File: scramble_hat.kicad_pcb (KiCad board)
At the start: 4 copper layers, 51.4 x 21.1 mm, 75 parts, among them J1 NCJ6FA-H, J2 TRRS PJ-3X4S (CTIA, bottom-si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, J3 Carrier LEFT 1-7, J4 Carrier RIGHT 1-7, J5 VDD_PoE / PGND, J6 I2C 3V3/AGND/SDA/SCL, K1 KAQY214S, K2 KAQY214S, Q1 DMP3098 (P-FET 60V), SW1 SS-12D00-G3, U1 ES8389, U2 TPS7A2033, U3 TLV9061, U4 74HC4053

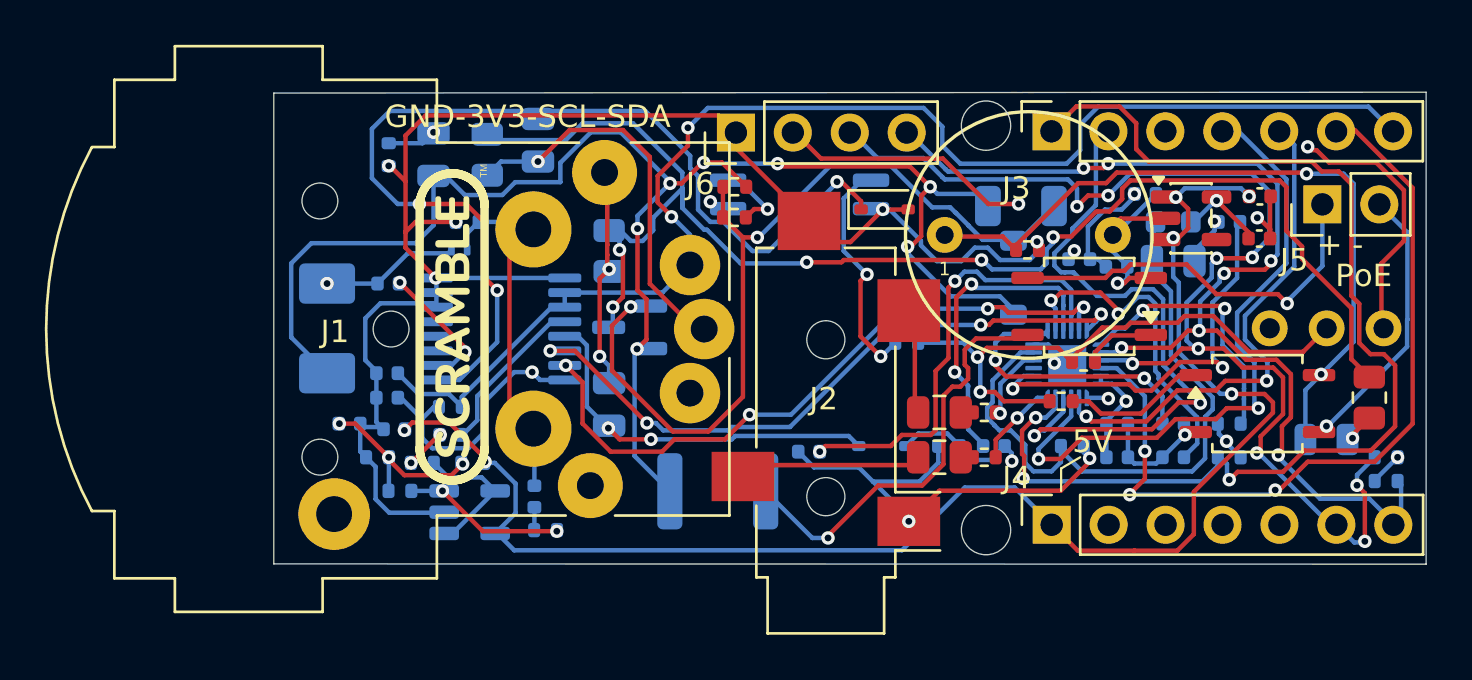
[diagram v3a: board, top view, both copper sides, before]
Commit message: sw1 optional: DNP by default (phantom-less builds); J7/R27 placed+routed; restore pos-file exclusions; regen fab + docs
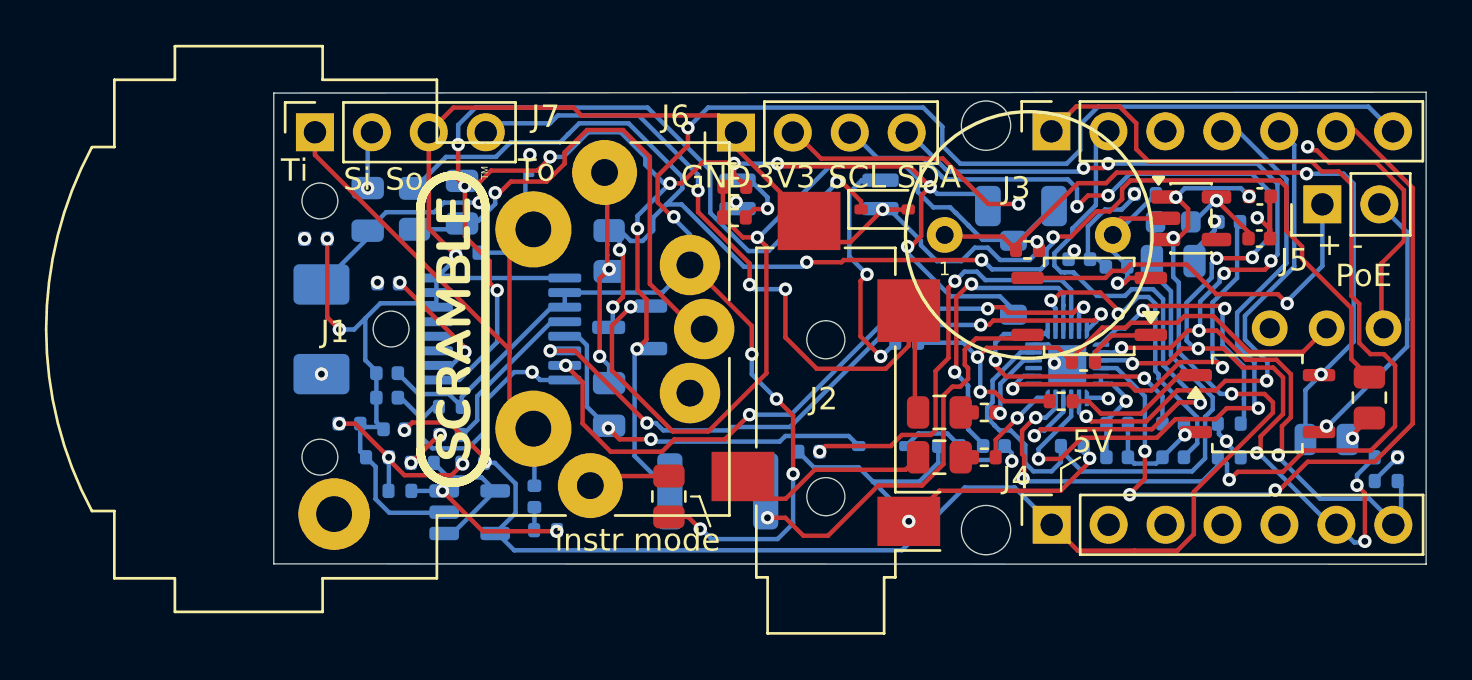
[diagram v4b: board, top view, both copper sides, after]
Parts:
- added J7: TO EURORACK MODULE (alt. to J1), Connector_PinSocket_2.54mm:PinSocket_1x04_P2.54mm_Vertical, F.Cu at (82.7, 82.0)
- added R27: R0 (force instrument mode), Resistor_SMD:R_0805_2012Metric, F.Cu at (98.5, 98.2)
- moved R25 4.96 mm to (82.8, 86.8), turned to 0 degrees
- moved D9 4.87 mm to (92.2, 83.5), turned to 90 degrees
- moved C11 4.37 mm to (89.3, 85.1)
- moved R6 4.04 mm to (87.2, 85.4)
- moved C17 3.82 mm to (85.1, 85.4)
- moved R26 1.37 mm to (89.5, 87.4)
- moved OK1 0.42 mm to (104.8, 84.8)
- moved D6 0.25 mm to (83.0, 90.8), turned to 90 degrees
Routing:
- net HP_L_OUT: track 3.20 -> 31.8 mm, vias 0 -> 3
- net DET: track 59.7 -> 79.4 mm, vias 2 -> 6
- net GTIP: track 15.5 -> 28.3 mm
- net V_FILT: track 70.9 -> 61.5 mm, vias 7 -> 9
- net MIC1N_XLR: track 45.3 -> 37.9 mm, vias 3 -> 4
- net XLR3_COLD: track 17.5 -> 22.3 mm
- net V_PHANTOM: track 62.9 -> 66.0 mm
- net PGND: track 42.2 -> 39.9 mm, vias 5 -> 8
- net AGND: track 113.9 -> 115.8 mm
- net HP_R_OUT: track 7.69 -> 8.99 mm
- net Q1_GATE: track 37.9 -> 38.8 mm
- net V_PoE: track 19.1 -> 18.4 mm
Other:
- board text added: "3V3"
- board text added: "GND"
- board text added: "Hat-trik v4"
- board text added: "SCL"
- board text added: "SDA"
- board text added: "Si"
- board text added: "So"
- board text added: "Ti"
- board text added: "To"
- board text removed: "GND-3V3-SCL-SDA"
- board text removed: "Hat-trik v3"

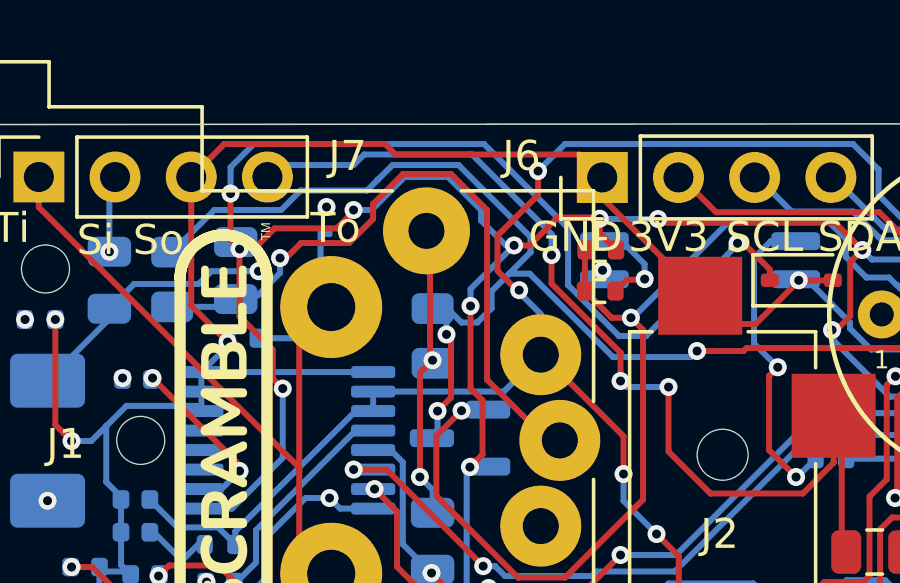
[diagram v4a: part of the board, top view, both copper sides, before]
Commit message: pcb: widen HP_L_OUT to MIC1N_XLR spacing on B.Cu; regen fab
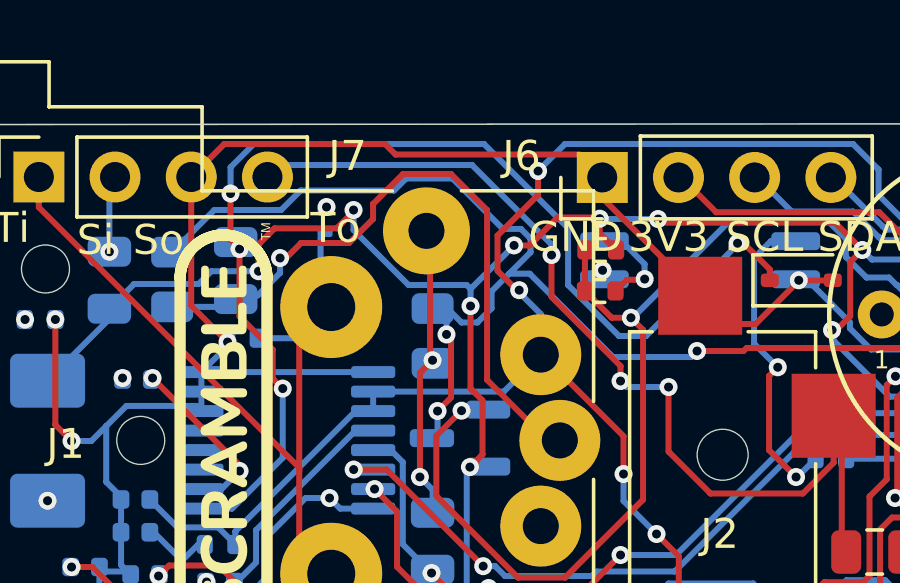
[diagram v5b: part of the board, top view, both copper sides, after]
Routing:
- net V_FILT: track 61.5 -> 60.0 mm
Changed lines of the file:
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@@
 	)
 	(segment
-		(start 102.1 87.855883)
-		(end 99.8 85.555883)
+		(start 109.474 91.3638)
+		(end 109.474 94.3532)
 		(width 0.2)
 		(layer "F.Cu")
@@
 	)
 	(segment
-		(start 109.474 91.3638)
-		(end 109.474 94.3532)
+		(start 109.2032 89.9582)
+		(end 109.2032 91.524618)
 		(width 0.2)
 		(layer "F.Cu")
@@
 	)
 	(segment
-		(start 109.2032 89.9582)
-		(end 109.2032 91.524618)
+		(start 102.1 88.8)
+		(end 102.1 88.3)
 		(width 0.2)
 		(layer "F.Cu")
@@
 	)
 	(segment
-		(start 99.8 85.555883)
+		(start 99.8 86)
 		(end 99.8 84.6)
 		(width 0.2)
@@
 	)
 	(segment
-		(start 102.1 88.8)
-		(end 102.1 87.855883)
+		(start 102.1 88.3)
+		(end 99.8 86)
 		(width 0.2)
 		(layer "F.Cu")
@@
 	)
 	(segment
-		(start 90.73 81.6)
-		(end 90.33 82)
-		(width 0.2)
-		(layer "B.Cu")
-		(net "HP_L_OUT")
-	)
-	(segment
-		(start 93.2 81.6)
-		(end 90.73 81.6)
-		(width 0.2)
-		(layer "B.Cu")
-		(net "HP_L_OUT")
-	)
-	(segment
 		(start 99.8 84.6)
-		(end 99.8 83.9)
+		(end 99.8 84.25)
 		(width 0.2)
 		(layer "B.Cu")
@@
 	)
 	(segment
-		(start 97.15 81.25)
-		(end 93.55 81.25)
+		(start 90.73 81.6)
+		(end 90.33 82)
 		(width 0.2)
 		(layer "B.Cu")
@@
 	)
 	(segment
-		(start 93.55 81.25)
-		(end 93.2 81.6)
+		(start 103.7 89)
+		(end 102.3 89)
 		(width 0.2)
 		(layer "B.Cu")
@@
 	)
 	(segment
-		(start 103.7 89)
-		(end 102.3 89)
+		(start 97.15 81.6)
+		(end 90.73 81.6)
 		(width 0.2)
 		(layer "B.Cu")
@@
 	)
 	(segment
-		(start 99.8 83.9)
-		(end 97.15 81.25)
+		(start 102.3 89)
+		(end 102.1 88.8)
 		(width 0.2)
 		(layer "B.Cu")
@@
 	)
 	(segment
-		(start 102.3 89)
-		(end 102.1 88.8)
+		(start 99.8 84.25)
+		(end 97.15 81.6)
 		(width 0.2)
 		(layer "B.Cu")
@@
 	)
 	(segment
+		(start 98.18 83.73)
+		(end 96.5 82.05)
+		(width 0.2)
+		(layer "B.Cu")
+		(net "V_PHANTOM")
+	)
+	(segment
+		(start 98.777818 83.73)
+		(end 98.18 83.73)
+		(width 0.2)
+		(layer "B.Cu")
+		(net "V_PHANTOM")
+	)
+	(segment
 		(start 96.8 86.85)
 		(end 97.327818 86.85)
@@
 	)
 	(segment
+		(start 90.785635 83.1)
+		(end 88.558521 83.1)
+		(width 0.2)
+		(layer "B.Cu")
+		(net "V_PHANTOM")
+	)
+	(segment
 		(start 115.674839 86.705862)
 		(end 115.643067 86.67409)
@@
 	)
 	(segment
-		(start 94.015 82.085)
-		(end 93.65 82.45)
+		(start 99.1 84.052182)
+		(end 98.777818 83.73)
+		(width 0.2)
+		(layer "B.Cu")
+		(net "V_PHANTOM")
+	)
+	(segment
+		(start 94.95 82.05)
+		(end 94.55 82.45)
+		(width 0.2)
+		(layer "B.Cu")
+		(net "V_PHANTOM")
+	)
+	(segment
+		(start 88.558521 83.1)
+		(end 87.154544 84.503977)
 		(width 0.2)
 		(layer "B.Cu")
@@
 	)
 	(segment
-		(start 93.65 82.45)
-		(end 91.435635 82.45)
+		(start 99.1 84.51)
+		(end 99.1 84.052182)
 		(width 0.2)
 		(layer "B.Cu")
@@
 	)
 	(segment
+		(start 94.55 82.45)
+		(end 91.435635 82.45)
+		(width 0.2)
+		(layer "B.Cu")
+		(net "V_PHANTOM")
+	)
+	(segment
 		(start 95.8342 86.3854)
 		(end 96.3354 86.3854)
@@
 	)
 	(segment
-		(start 96.298847 87.2479)
-		(end 96.298847 86.850047)
+		(start 98.387899 85.222101)
+		(end 99.1 84.51)
 		(width 0.2)
 		(layer "B.Cu")
@@
 	)
 	(segment
-		(start 97.8 85.81)
-		(end 98.387899 85.222101)
+		(start 96.298847 87.2479)
+		(end 96.298847 86.850047)
 		(width 0.2)
 		(layer "B.Cu")
@@
 	)
 	(segment
-		(start 94.5 81.6)
-		(end 94.015 82.085)
+		(start 97.8 85.81)
+		(end 98.387899 85.222101)
 		(width 0.2)
 		(layer "B.Cu")
@@
 	)
 	(segment
-		(start 88.558521 83.1)
-		(end 87.154544 84.503977)
-		(width 0.2)
-		(layer "B.Cu")
-		(net "V_PHANTOM")
-	)
-	(segment
-		(start 94.015 82.085)
-		(end 94 82.085)
+		(start 91.435635 82.45)
+		(end 90.785635 83.1)
 		(width 0.2)
 		(layer "B.Cu")
@@
 	)
 	(segment
-		(start 90.785635 83.1)
-		(end 88.558521 83.1)
-		(width 0.2)
-		(layer "B.Cu")
-		(net "V_PHANTOM")
-	)
-	(segment
-		(start 96.7 81.6)
-		(end 94.5 81.6)
-		(width 0.2)
-		(layer "B.Cu")
-		(net "V_PHANTOM")
-	)
-	(segment
 		(start 99.072101 85.222101)
 		(end 101.85 88)
@@
 	)
 	(segment
-		(start 91.435635 82.45)
-		(end 90.785635 83.1)
-		(width 0.2)
-		(layer "B.Cu")
-		(net "V_PHANTOM")
-	)
-	(segment
 		(start 97.8 86.377818)
 		(end 97.8 85.81)
@@
 	)
 	(segment
-		(start 99.1 84)
-		(end 96.7 81.6)
-		(width 0.2)
-		(layer "B.Cu")
-		(net "V_PHANTOM")
-	)
-	(segment
 		(start 104.45 88)
 		(end 104.65 87.8)
@@
 	)
 	(segment
-		(start 96.298847 86.850047)
-		(end 95.8342 86.3854)
+		(start 96.5 82.05)
+		(end 94.95 82.05)
 		(width 0.2)
 		(layer "B.Cu")
@@
 	)
 	(segment
-		(start 98.387899 85.222101)
-		(end 99.1 84.51)
-		(width 0.2)
-		(layer "B.Cu")
-		(net "V_PHANTOM")
-	)
-	(segment
-		(start 99.1 84.51)
-		(end 99.1 84)
+		(start 96.298847 86.850047)
+		(end 95.8342 86.3854)
 		(width 0.2)
 		(layer "B.Cu")
@@
 	)
 	(segment
-		(start 98.28 84.28)
-		(end 98.55 84.28)
-		(width 0.2)
-		(layer "B.Cu")
-		(net "V_FILT")
-	)
-	(segment
 		(start 110.4766 84.75)
 		(end 112.275 84.75)
@@
 	)
 	(segment
-		(start 97.45 83.1)
-		(end 97.45 83.45)
-		(width 0.2)
-		(layer "B.Cu")
-		(net "V_FILT")
-	)
-	(segment
 		(start 88.033523 85.566477)
 		(end 85.886022 85.566477)
@@
 	)
 	(segment
-		(start 97.45 83.45)
-		(end 98.28 84.28)
-		(width 0.2)
-		(layer "B.Cu")
-		(net "V_FILT")
-	)
-	(segment
 		(start 109.19501 87.14501)
 		(end 109.19501 87.44501)
@@
 	)
 	(segment
-		(start 93.2 83.1)
-		(end 93.8 83.1)
+		(start 95.032236 85.6)
+		(end 93.2 83.767764)
 		(width 0.2)
 		(layer "B.Cu")
@@
 	)
 	(segment
-		(start 111.070701 89.320701)
-		(end 113.270701 89.320701)
+		(start 93.2 83.767764)
+		(end 93.2 83.1)
 		(width 0.2)
 		(layer "B.Cu")
@@
 	)
 	(segment
-		(start 96.35 82)
-		(end 97.45 83.1)
+		(start 111.070701 89.320701)
+		(end 113.270701 89.320701)
 		(width 0.2)
 		(layer "B.Cu")
@@
 	)
 	(segment
-		(start 93.8 83.1)
-		(end 94.9 82)
+		(start 96.97 85.6)
+		(end 95.032236 85.6)
 		(width 0.2)
 		(layer "B.Cu")
@@
 	)
 	(segment
-		(start 94.9 82)
-		(end 96.35 82)
+		(start 97.1 85.73)
+		(end 96.97 85.6)
 		(width 0.2)
 		(layer "B.Cu")

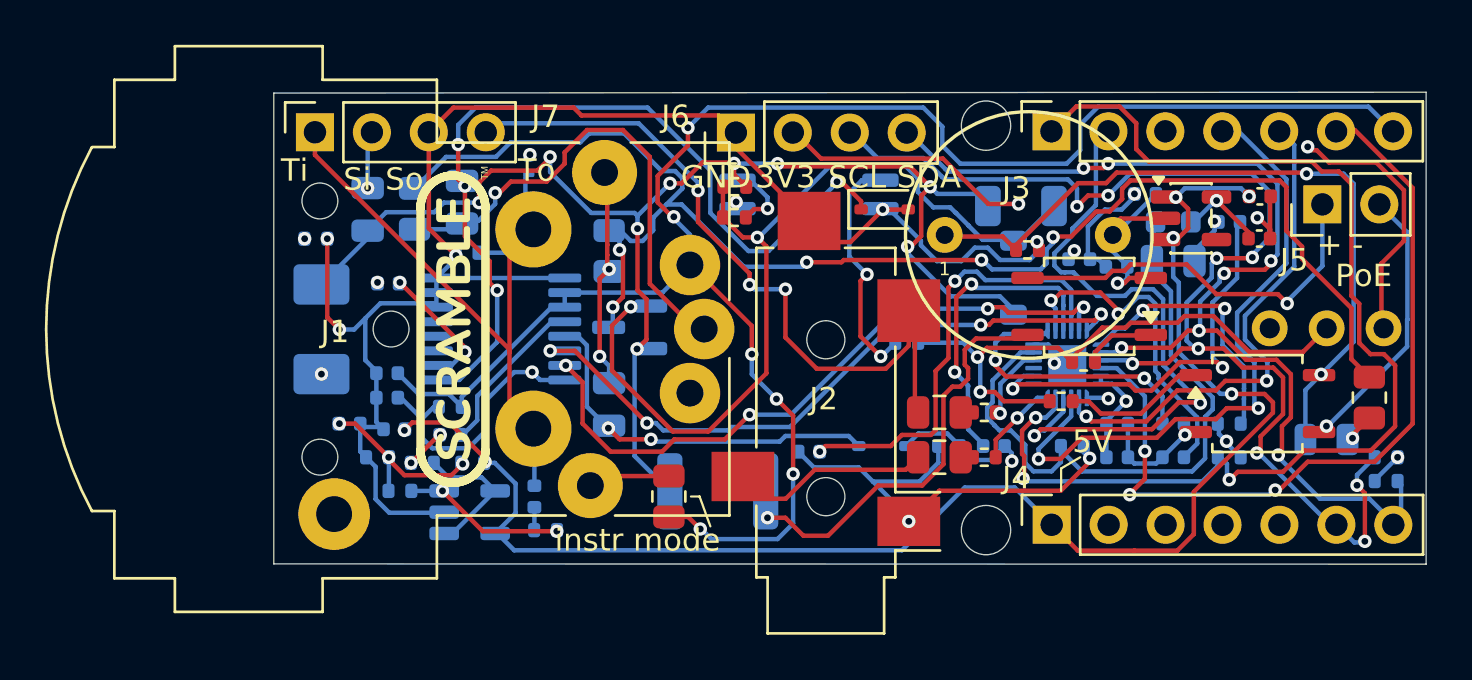
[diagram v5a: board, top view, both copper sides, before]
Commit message: pcb: place + route C30 phantom-rail bypass; restore pos-file exclusions; regen fab
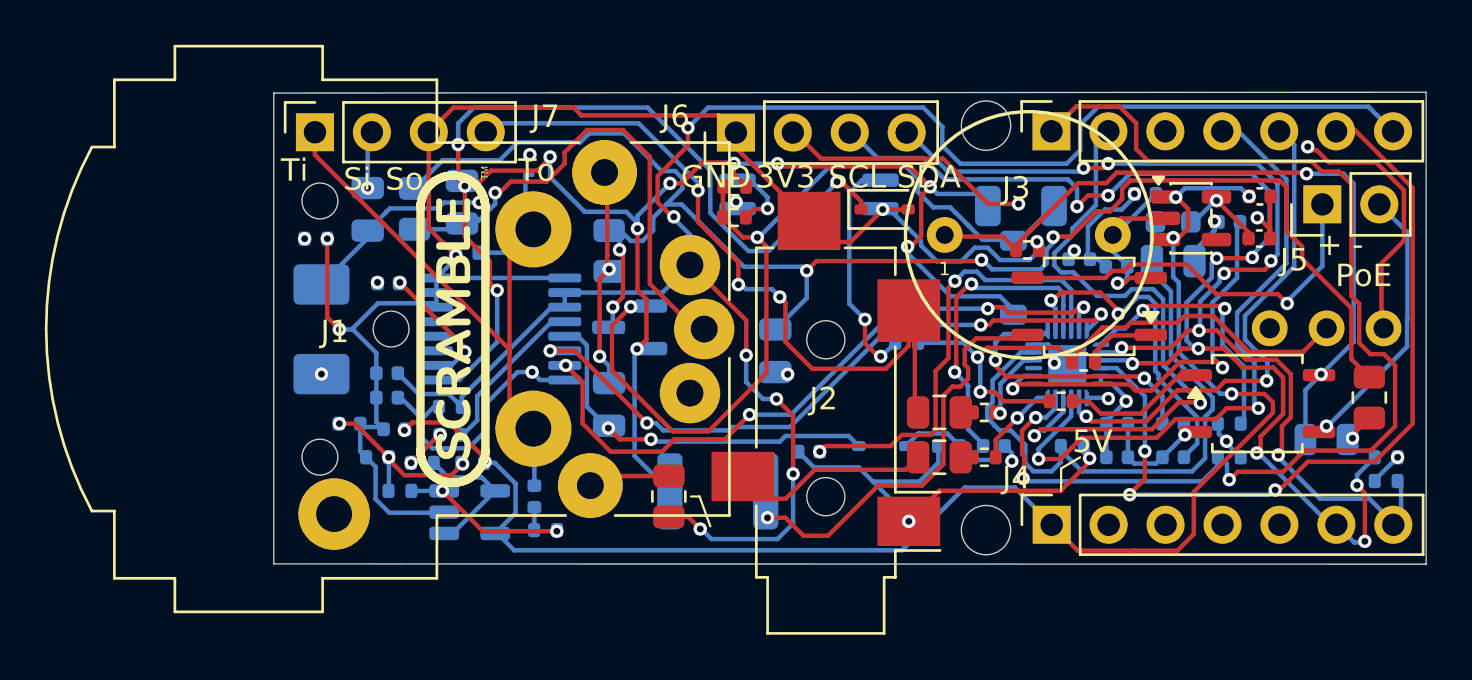
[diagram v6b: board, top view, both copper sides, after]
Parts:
- added C30: 100nF 100V, Capacitor_SMD:C_0805_2012Metric, B.Cu at (103.2, 91.8)
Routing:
- net V_PHANTOM: track 65.5 -> 68.9 mm
- net PGND: track 39.9 -> 40.5 mm, vias 8 -> 9
- net V_FILT: track 60.0 -> 60.5 mm

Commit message: pcb: reroute pass on input section; regen fab
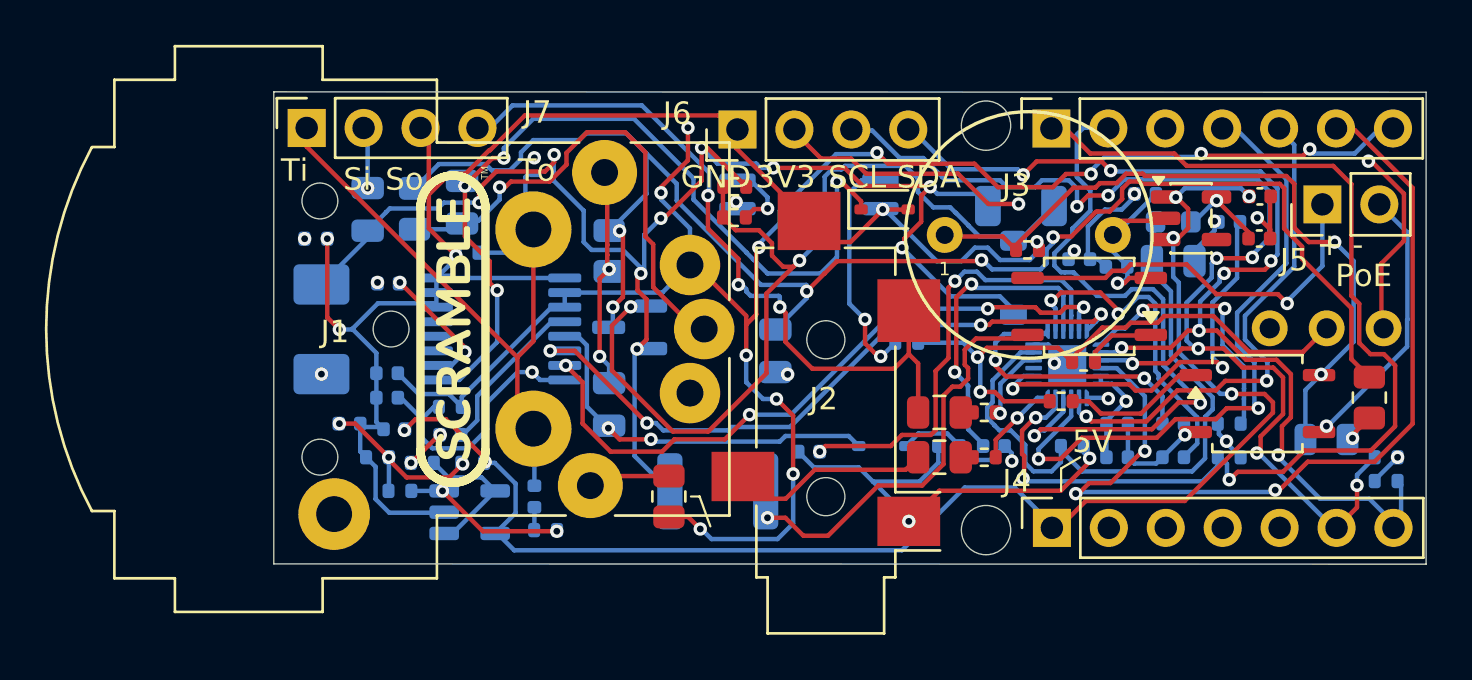
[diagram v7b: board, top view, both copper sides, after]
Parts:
- moved J7 0.42 mm to (82.3, 81.8)
- moved D9 0.25 mm to (92.5, 83.5)
- moved J6 0.15 mm to (101.6, 81.9)
- moved J4 0.14 mm to (115.6, 99.7)
- moved J3 0.13 mm to (115.6, 81.8)
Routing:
- net V_FILT: track 60.5 -> 64.9 mm
- net MCLK: track 36.1 -> 40.2 mm
- net AGND: track 115.7 -> 113.4 mm
- net Q1_GATE: track 38.8 -> 41.1 mm
- net SCL: track 54.9 -> 52.7 mm, vias 9 -> 8
- net +5V: track 67.7 -> 65.8 mm
- net GTIP: track 28.3 -> 30.1 mm
- net ASDOUT: track 51.5 -> 50.0 mm
- net LRCK: track 28.7 -> 29.9 mm
- net HP_L_OUT: track 31.4 -> 32.5 mm
- net PGND: track 40.5 -> 39.6 mm
- net V_PHANTOM: track 68.9 -> 68.1 mm
- net DET: track 79.8 -> 80.5 mm, vias 6 -> 11
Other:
- outline, holes or cut-outs redrawn
